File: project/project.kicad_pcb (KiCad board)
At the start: 6 copper layers, 45 x 115 mm, 235 parts, among them IC1 ESP32-C61-WROOM-1-N8R2, IC10 TLV320AIC3104IRHBR, IC11 TPA2005D1DGNR, IC12 MAX17262REWL+T, IC3 STPMIC1DPQR, IC4 ST1S31PUR, IC5 MCP23017-E_ML, IC6 TPS2117DRLR, IC7 ECMF02-2AMX6, IC8 TCPP01-M12, IC9 MT41K128M16JT-107_K, J1 Micro_SD_Card_Det2, J2 OMTP, Q2 STL11N3LLH6, SW1 PTS636SM43SMTR LFS, SW2 SW_DIP_x04, SW3 PTS636SM43SMTR LFS, U1 STM32MP135F, U2 USB C DRP, U3 MCP73831-2-OT, U5 EMIF06-MSD02N16, Y1 Crystal 24 MHz, Y2 Crystal 32.67 KHz

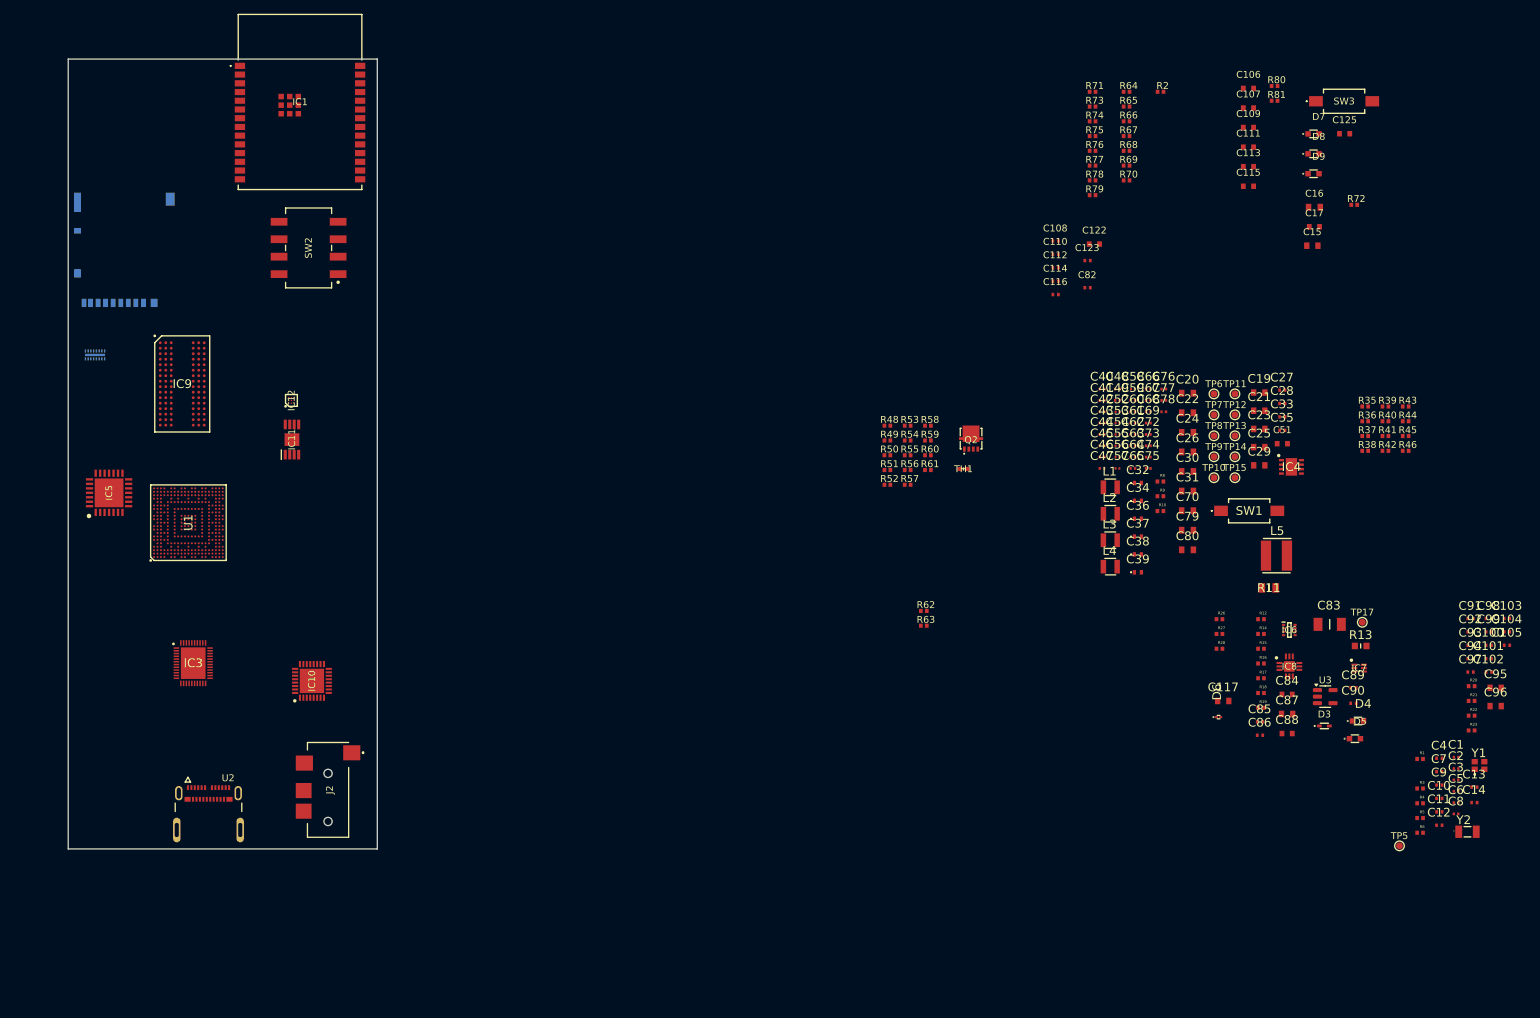
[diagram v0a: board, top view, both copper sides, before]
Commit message: schemtic is done, annotation set
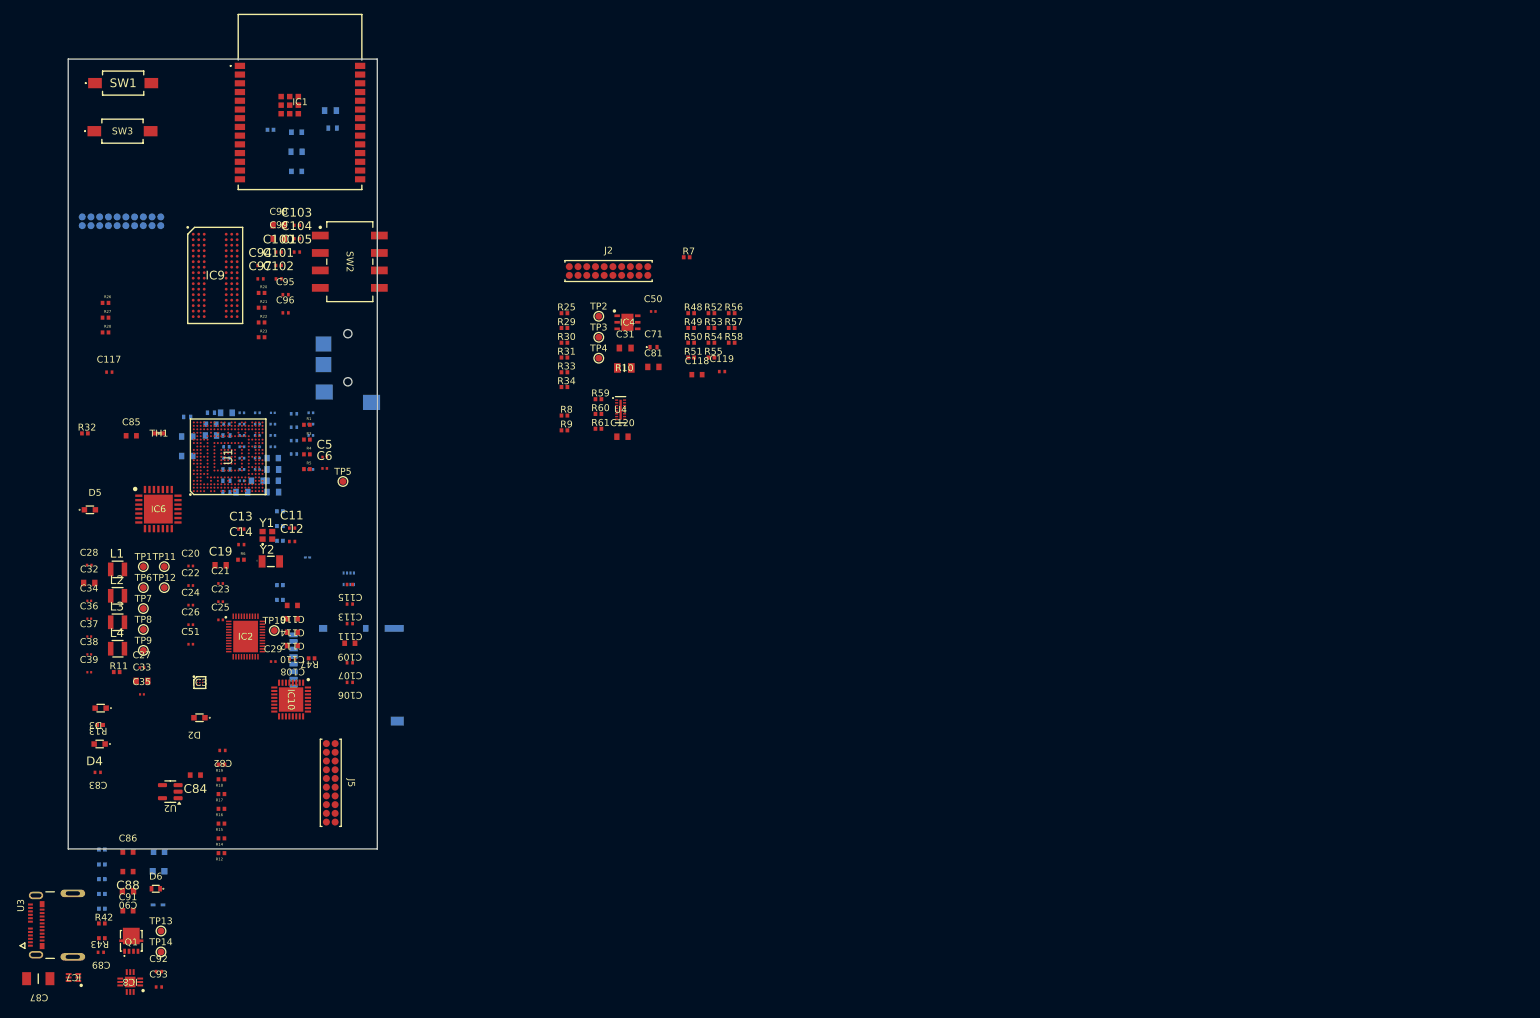
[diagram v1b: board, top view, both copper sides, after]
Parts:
- removed C122, C125: 100nF, bozi:GRM18_T10
- removed C123: 1uF, bozi:GRM15_T05
- removed C30: 22uF, bozi:GRM18_T20
- removed C57: 1nF, bozi:GRM03_T03
- removed IC11: TPA2005D1DGNR, bozi:SOP65P490X110-9N
- removed IC12: MAX17262REWL+T, bozi:BGA9C40P3X3_147X145X69
- removed L5: 2.2uH, bozi:INDPM4040X250N_edit
- removed Q2: STL11N3LLH6, bozi:STL20N6F7_edit
- removed R62, R63: 2.4K, bozi:RESC1005X37N_edit
- removed R64, R65, R66, R67, R68, R69, R70, R71, R72, R73, R74, R75, R76, R77, R78, R79, R80, R81: 0R, bozi:RESC1005X37N_edit
- removed TP15, TP17: TestPoint, TestPoint:TestPoint_Pad_D1.0mm
- removed U5: EMIF06-MSD02N16, bozi:MICROQFN16_1P25X3P55X0P4_STM_edit
- added C118: 100nF, bozi:GRM18_T10, F.Cu at (176.5, 78.5)
- added C119: 1uF, bozi:GRM15_T05, F.Cu at (180.2, 78.0)
- added C120: 10uF, bozi:GRT18_T15, F.Cu at (165.7, 87.5)
- added C18: 100nF, bozi:GRM18_T10, B.Cu at (118.2, 48.9)
- added C50: 1uF, bozi:GRM03_T09, F.Cu at (170.2, 69.2)
- added C71: 4.7uF, bozi:GRM15_T15, F.Cu at (170.2, 74.4)
- added C81: 10uF, bozi:GRT18_T15, F.Cu at (170.2, 77.3)
- added D1: TVS 22VWM 41VC, bozi:ESDA25P351U1M_edit, B.Cu at (123.5, 42.5)
- added D2: LED, bozi:LEDC1608X70N_edit, F.Cu at (104.1, 128.4)
- added IC2: STPMIC1DPQR, bozi:QFN40P500X600X80-45N-D_edit, F.Cu at (110.8, 116.6)
- added J3: CTIA, bozi:SJ23574ASMTTR, B.Cu at (126.0, 77.1)
- added J4: Micro_SD_Card_Det2, Connector_Card:microSD_HC_Hirose_DM3AT-SF-PEJM5, B.Cu at (125.5, 122.2)
- added J5: POGO header keypad & power, bozi:8552202030001101_edit, F.Cu at (123.2, 137.9)
- added Q1: STL11N3LLH6, bozi:STL20N6F7_edit, F.Cu at (94.2, 160.9)
- added R24: 100R, bozi:RESC1005X37N_edit, B.Cu at (115.8, 111.2)
- added R25: 100R, bozi:RESC1005X37N_edit, F.Cu at (157.2, 69.5)
- added R29: 10k, bozi:RESC1005X37N_edit, F.Cu at (157.2, 71.7)
- added R30: 10k, bozi:RESC1005X37N_edit, F.Cu at (157.2, 73.8)
- added R31: 1k, bozi:RESC1005X37N_edit, F.Cu at (157.2, 76.0)
- added R32: 1k, bozi:RESC1005X37N_edit, F.Cu at (87.4, 87.0)
- added R33: 1k, bozi:RESC1005X37N_edit, F.Cu at (157.2, 78.1)
- added R34: 1k, bozi:RESC1005X37N_edit, F.Cu at (157.2, 80.2)
- added R47: 240R, bozi:RESC1005X37N_edit, F.Cu at (120.4, 119.8)
- added R7: 0R, bozi:RESC1005X37N_edit, F.Cu at (175.0, 61.4)
- added TP1: TestPoint, TestPoint:TestPoint_Pad_D1.0mm, F.Cu at (95.9, 106.4)
- added TP2: TestPoint, TestPoint:TestPoint_Pad_D1.0mm, F.Cu at (162.2, 70.0)
- added TP3: TestPoint, TestPoint:TestPoint_Pad_D1.0mm, F.Cu at (162.2, 73.0)
- added TP4: TestPoint, TestPoint:TestPoint_Pad_D1.0mm, F.Cu at (162.2, 76.0)
- added U4: EMIF06-MSD02N16, bozi:MICROQFN16_1P25X3P55X0P4_STM_edit, F.Cu at (165.4, 83.6)
- C1, C10, C2, C3, C4, C41, C42, C43, C48, C49, C59, C60, C61, C62, C63, C64, C7, C8, C9, D8, R35: moved to B.Cu
- C106, C107: footprint bozi:GRM18_T10 -> bozi:GRM15_T05
- C108: value 1uF -> 100nF
- C110, C112, C114, C116: value 1uF -> 100nF; footprint bozi:GRM15_T05 -> bozi:GRM18_T10
- C111, C113, C115: value 100nF -> 1uF; footprint bozi:GRM18_T10 -> bozi:GRM15_T05
- C117: value 10uF -> 1uF; footprint bozi:GRT18_T15 -> bozi:GRM15_T05
- C15: value 10uF -> 22uF; footprint bozi:GRT18_T15 -> bozi:GRM18_T20; moved to B.Cu
- C16: value 22uF -> 100nF; footprint bozi:GRM18_T20 -> bozi:GRM18_T10; moved to B.Cu
- C17: value 100nF -> 10uF; footprint bozi:GRM18_T10 -> bozi:GRT18_T15; moved to B.Cu
- C20, C22, C24, C26: value 22uF -> 1uF; footprint bozi:GRM18_T20 -> bozi:GRM03_T09
- C21, C23, C25, C29: value 10uF -> 1uF; footprint bozi:GRT18_T15 -> bozi:GRM03_T09
- C27, C28: footprint bozi:GRM15_T05 -> bozi:GRM03_T09
- C32: value 4.7uF -> 10uF; footprint bozi:GRM15_T15 -> bozi:GRT18_T15
- C33: value 1uF -> 22uF; footprint bozi:GRM15_T05 -> bozi:GRM18_T20
- C34, C36, C37, C38, C39: value 4.7uF -> 1nF; footprint bozi:GRM15_T15 -> bozi:GRM03_T03
- C35: value 1uF -> 1nF; footprint bozi:GRM15_T05 -> bozi:GRM03_T03
- C40: value 1uF -> 1nF; footprint bozi:GRM03_T09 -> bozi:GRM03_T03; moved to B.Cu
- C44, C46: value 1uF -> 10uF; footprint bozi:GRM03_T09 -> bozi:GRT18_T15; moved to B.Cu
- C45, C47, C65, C66: value 1uF -> 22uF; footprint bozi:GRM03_T09 -> bozi:GRM18_T20; moved to B.Cu
- C51: value 100nF -> 1uF; footprint bozi:GRM18_T10 -> bozi:GRM03_T09
- C52, C53, C54, C55, C58: value 1nF -> 1uF; footprint bozi:GRM03_T03 -> bozi:GRM03_T09; moved to B.Cu
- C56: value 1nF -> 22uF; footprint bozi:GRM03_T03 -> bozi:GRM18_T20; moved to B.Cu
- C67, C69, C72: footprint bozi:GRM03_T09 -> bozi:GRM15_T05; moved to B.Cu
- C68, C73, C74, C75, C76: value 1uF -> 4.7uF; footprint bozi:GRM03_T09 -> bozi:GRM15_T15; moved to B.Cu
- C70: value 22uF -> 4.7uF; footprint bozi:GRM18_T20 -> bozi:GRM15_T15; moved to B.Cu
- C77: value 1uF -> 100nF; footprint bozi:GRM03_T09 -> bozi:GRM18_T10; moved to B.Cu
- C78: value 1uF -> 4.7uF; footprint bozi:GRM03_T09 -> bozi:GRM18_T15; moved to B.Cu
- C79: value 22uF -> 4.7uF; footprint bozi:GRM18_T20 -> bozi:GRM18_T15; moved to B.Cu
- C80: value 22uF -> 10uF; footprint bozi:GRM18_T20 -> bozi:GRT18_T15; moved to B.Cu
- C82: value 1uF -> 470pF; footprint bozi:GRM15_T05 -> bozi:GRT15_T05
- C83: value 220uF -> 1uF; footprint bozi:GRM31_T30 -> bozi:GRM15_T05
- C84: value 2.2uF -> 100nF
- C85: value 4.7uF -> 100nF; footprint bozi:GRM15_T05 -> bozi:GRM18_T10
- C86: value 4.7uF -> 2.2uF; footprint bozi:GRM15_T05 -> bozi:GRM18_T10
- C87: value 4.7uF -> 220uF; footprint bozi:GRM18_T15 -> bozi:GRM31_T30
- C88: value 100nF -> 100pF
- C89: value 470pF -> 1uF; footprint bozi:GRT15_T05 -> bozi:GRM15_T05
- C90: value 470pF -> 4.7uF; footprint bozi:GRT15_T05 -> bozi:GRM18_T15
- C91: footprint bozi:GRM15_T05 -> bozi:GRM18_T10
- C92, C93: value 100nF -> 470pF; footprint bozi:GRM15_T05 -> bozi:GRT15_T05
- C95, C96: value 10uF -> 100nF; footprint bozi:GRT18_T15 -> bozi:GRM15_T05
- C98, C99: value 100nF -> 10uF; footprint bozi:GRM15_T05 -> bozi:GRT18_T15
- D3: value BAT54KFILM -> LED; footprint bozi:SODFL1608X70N_edit -> bozi:LEDC1608X70N_edit
- D6: value ESDALC6V1-1U2 -> TVS 22VWM 41VC; footprint bozi:ESDALC6V11U2_edit -> bozi:ESDA25P351U1M_edit
- D7: value LED -> BAT54KFILM; footprint bozi:LEDC1608X70N_edit -> bozi:SODFL1608X70N_edit; moved to B.Cu
- D9: value LED -> ESDALC6V1-1U2; footprint bozi:LEDC1608X70N_edit -> bozi:ESDALC6V11U2_edit; moved to B.Cu
- IC3: value STPMIC1DPQR -> MAX17262REWL+T; footprint bozi:QFN40P500X600X80-45N-D_edit -> bozi:BGA9C40P3X3_147X145X69
- IC4: value ST1S31PUR -> LD39200PU33R; footprint bozi:SON65P300X300X100-9N-D_edit -> bozi:SON95P300X300X100-7N-D
- IC5: value MCP23017-E_ML -> TPS2117DRLR; footprint bozi:QFN65P600X600X100-29N-D_edit -> bozi:SOTFL50P160X60-8N; moved to B.Cu
- IC6: value TPS2117DRLR -> MCP23017-E_ML; footprint bozi:SOTFL50P160X60-8N -> bozi:QFN65P600X600X100-29N-D_edit
- J1: value Micro_SD_Card_Det2 -> POGO header 20 pin; footprint Connector_Card:microSD_HC_Hirose_DM3AT-SF-PEJM5 -> bozi:8552202030001101_edit
- J2: value OMTP -> POGO header display; footprint bozi:SJ23574ASMTTR -> bozi:8552202030001101_edit
- R1, R3: value 2.4K -> 2.4k
- R10: value 24k -> 100m; footprint bozi:RESC1005X37N_edit -> bozi:RESC2012X60N_edit
- R11: value 100m -> 0R; footprint bozi:RESC2012X60N_edit -> bozi:RESC1005X37N_edit
- R12, R23: value 240R -> 0R
- R13: value 1R -> 0R; footprint bozi:RESC1608X55N_edit -> bozi:RESC1005X37N_edit
- R14, R20, R21: value 10K -> 0R
- R15: value 47K -> 1k
- R16: value 47K -> 240R
- R17: value 2.4K -> 1k
- R18, R19: value 5.1K -> 0R
- R2: value 0R -> 2.4k; moved to B.Cu
- R22: value 100R -> 0R
- R26: value 10K -> 100R
- R27: value 10K -> 10k
- R28: value 100K -> 10k
- R36: value 100R -> 240R; moved to B.Cu
- R37: value 100R -> 1R; footprint bozi:RESC1005X37N_edit -> bozi:RESC1608X55N_edit; moved to B.Cu
- R38: value 1K -> 10k; moved to B.Cu
- R39: value 1K -> 2.4k; moved to B.Cu
- R4: value 3K -> 2.4k
- R40, R41: value 1K -> 47k; moved to B.Cu
- R42: value 10K -> 5.1k
- R43: value 100R -> 5.1k
- R44, R45: value 10K -> 10k; moved to B.Cu
- R46: value 10K -> 100R; moved to B.Cu
- R48: value 30R -> 1k
- R49, R50, R51, R52, R53, R54, R55, R56, R57, R58: value 30R -> 0R
- R5: value 240R -> 3k
- R59, R60: value 30R -> 10k
- R6: value 0R -> 240R
- R61: value 30R -> 100k
- R8: value 560R -> 0R
- R9: value 75k -> 10k
- TH1: value 10K NTC -> 10k NTC
- U2: value USB C DRP -> MCP73831-2-OT; footprint bozi:2012670005_edit -> Package_TO_SOT_SMD:SOT-23-5
- U3: value MCP73831-2-OT -> USB C DRP; footprint Package_TO_SOT_SMD:SOT-23-5 -> bozi:2012670005_edit
- moved R43 205.0 mm to (89.9, 160.5), turned to 180 degrees
- moved D7 202.2 mm to (98.1, 155.7)
- moved C91 200.1 mm to (93.7, 156.5)
- moved R39 199.1 mm to (89.9, 151.9), turned to 180 degrees
- moved R40 199.1 mm to (89.9, 154.1), turned to 180 degrees
- moved R41 199.1 mm to (89.9, 156.2), turned to 180 degrees
- moved R42 199.1 mm to (89.9, 158.3)
- moved C93 197.3 mm to (98.2, 167.6)
- moved C92 197.3 mm to (98.2, 165.3)
- moved D8 196.4 mm to (98.2, 148.0)
- moved R36 194.2 mm to (89.9, 147.6)
- moved R38 193.5 mm to (89.9, 149.8), turned to 180 degrees
- moved IC7 192.5 mm to (85.8, 166.2), turned to 180 degrees
- moved D5 187.2 mm to (88.2, 98.1)
- moved R37 186.8 mm to (98.2, 150.8)
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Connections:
- C104 pad 1: VREF_DDR -> VDD_DDR
- C105 pad 1: VREF_DDR -> VDD_DDR
- C106 pad 1: Net-(U4-SEL) -> VDD_DDR
- C107 pad 1: Net-(IC10-DRVDD_1) -> VREF_DDR
- C108 pad 1: Net-(IC10-DRVDD_1) -> VREF_DDR
- C109 pad 1: Net-(IC10-DRVDD_1) -> Net-(IC10-MIC2R/LINE2R)
- C109 pad 2: GNDREF -> Net-(IC10-MIC2L/LINE2L/MICDET)
- C111 pad 1: Net-(IC10-AVDD) -> Net-(IC10-DRVDD_1)
- C112 pad 1: Net-(IC10-AVDD) -> Net-(IC10-DRVDD_1)
- C113 pad 1: Net-(IC10-IOVDD) -> Net-(IC10-DRVDD_1)
- C114 pad 1: Net-(IC10-IOVDD) -> Net-(IC10-AVDD)
- C115 pad 1: Net-(IC10-DVDD) -> Net-(IC10-AVDD)
- C116 pad 1: Net-(IC10-DVDD) -> Net-(IC10-IOVDD)
- C117 pad 1: VDD_SD -> Net-(IC10-IOVDD)
- C15 pad 1: VDD_3V3 -> Net-(IC1-3V3)
- C17 pad 1: Net-(IC1-3V3) -> 3V3_AO
- C19 pad 1: 5V_VIN -> VSYS
- C20 pad 1: VDD_CPU -> VDD
- C21 pad 1: 5V_VIN -> VDD
- C22 pad 1: VDD_DDR -> VDD
- C23 pad 1: 5V_VIN -> VDD
- C25 pad 1: 5V_VIN -> VDD
- C26 pad 1: VDD_CORE -> VDD
- C27 pad 1: VREF_DDR -> VDD
- C28 pad 1: 5V_VIN -> VDD
- C29 pad 1: 5V_VIN -> VDD
- C31 pad 1: 3V3_AO -> VDD_CPU
- C32 pad 1: VDD_ADC -> VSYS
- C33 pad 1: 5V_VIN -> VDD_DDR
- C34 pad 1: Net-(IC3-LDO2OUT) -> VDD_DDR
- C35 pad 1: 5V_VIN -> VDD_DDR
- C36 pad 1: VDD_SD -> VDD_DDR
- C37 pad 1: GNDREF -> VDD_DDR
- C37 pad 2: 5V_VIN -> GNDREF
- C38 pad 1: GNDREF -> VDD_DDR
- C38 pad 2: Net-(IC3-INTLDO) -> GNDREF
- C39 pad 1: Net-(IC3-LDO4OUT) -> VDD_DDR
- C40 pad 1: VDD -> VDD_DDR
- C41 pad 1: VDD -> VDD_DDR
- C42 pad 1: VDD -> VDD_DDR
- C43 pad 1: VDD -> VDD_DDR
- C44 pad 1: VDD -> VSYS
- C46 pad 1: VDD -> VSYS
- C47 pad 1: VDD -> VDD_CORE
- C48 pad 1: VDD -> VDD_CORE
- C49 pad 1: VDD -> VDD_CORE
- C51 pad 1: Net-(IC3-PONKEYN) -> VDD_CORE
- C52 pad 1: VDD_DDR -> VDD_CORE
- C53 pad 1: VDD_DDR -> VDD_CORE
- C54 pad 1: VDD_DDR -> VDD_CORE
- C55 pad 1: VDD_DDR -> VDD_CORE
- C56 pad 1: VDD_DDR -> VDD_CORE
- C58 pad 1: VDD_DDR -> VDD_CPU
- C59 pad 1: VDD_DDR -> VDD_CPU
- C60 pad 1: VDD_DDR -> VDD_CPU
- C61 pad 1: VDD_DDR -> VDD_CPU
- C62 pad 1: VDD_CORE -> VDD_CPU
- C63 pad 1: VDD_CORE -> VDD_CPU
- C64 pad 1: VDD_CORE -> VDD_CPU
- C65 pad 1: VDD_CORE -> VDD_CPU
- C66 pad 1: VDD_CORE -> VDD_CPU
- C67 pad 1: VDD_CORE -> VREF_DDR
- C68 pad 1: VDD_CORE -> VDD_ADC
- C69 pad 1: VDD_CORE -> VSYS
- C70 pad 1: VDD_CORE -> VDD_CODEC
- C72 pad 1: VDD_CPU -> VSYS
- C73 pad 1: VDD_CPU -> VDD_SD
- C74 pad 1: VDD_CPU -> GNDREF
- C74 pad 2: GNDREF -> VSYS
- C75 pad 1: VDD_CPU -> GNDREF
- C75 pad 2: GNDREF -> Net-(IC2-INTLDO)
- C76 pad 1: VDD_CPU -> Net-(IC2-LDO4OUT)
- C77 pad 1: VDD_CPU -> Net-(IC2-PONKEYN)
- C78 pad 1: VDD_CPU -> Net-(D2-A)
- C78 pad 2: GNDREF -> GND
- C79 pad 1: VDD_CPU -> Net-(U2-V_{BAT})
- C79 pad 2: GNDREF -> GND
- C80 pad 1: VDD_CPU -> 3V3_AO
- C82 pad 1: Net-(D2-K) -> Net-(IC3-REG)
- C83 pad 1: 5V_VIN -> Net-(IC6-VDD)
- C84 pad 1: Net-(IC8-GATE) -> Net-(IC6-VDD)
- C84 pad 2: Net-(D2-K) -> GNDREF
- C85 pad 1: Net-(BT1-+) -> /GPIO & IO expander/NRST
- C85 pad 2: GND -> GNDREF
- C86 pad 1: Net-(D5-A) -> Net-(IC8-GATE)
- C86 pad 2: GND -> Net-(D6-K)
- C87 pad 1: GNDREF -> 5V_VIN
- C87 pad 2: Net-(C87-Pad2) -> GNDREF
- C88 pad 1: GNDREF -> Net-(D6-K)
- C88 pad 2: Net-(D3-K) -> GND
- C89 pad 1: /USB C DRP/USB_CC1 -> Net-(D6-K)
- C89 pad 2: GNDREF -> GND
- C90 pad 1: /USB C DRP/USB_CC2 -> GNDREF
- C90 pad 2: GNDREF -> Net-(C90-Pad2)
- C91 pad 1: VDD_DDR -> GNDREF
- C91 pad 2: GNDREF -> Net-(D7-K)
- C92 pad 1: VDD_DDR -> /USB C DRP/USB_CC1
- C93 pad 1: VDD_DDR -> /USB C DRP/USB_CC2
- D3 pad 1: Net-(D3-K) -> GNDREF
- D3 pad 2: Net-(D2-K) -> Net-(D3-A)
- D5 pad 1: Net-(D5-K) -> GNDREF
- D6 pad 1: /MPU/SDMMC1_DETECT -> Net-(D6-K)
- D6 pad 2: GNDREF -> GND
- D7 pad 1: GNDREF -> Net-(D7-K)
- D7 pad 2: Net-(D7-A) -> Net-(D6-K)
- D9 pad 1: GNDREF -> /MPU/SDMMC1_GPIO0
- D9 pad 2: Net-(D9-A) -> GNDREF
- IC10 pad 1: Net-(IC10-MCLK) -> /MPU/RCC_MCO_1
- IC4 pad 1: 5V_VIN -> 3V3_AO
- IC4 pad 2: VDD -> 3V3_AO
- IC4 pad 3: Net-(IC4-FB) -> GNDREF
- IC4 pad 4: GNDREF -> /MPU/REG_3V3_GPIO0
- IC4 pad 5: Net-(IC4-PG) -> VSYS
- IC4 pad 6: 5V_VIN -> VSYS
- IC4 pad 7: Net-(IC4-SW) -> GNDREF
- IC5 pad 1: /GPIO & IO expander/GPB4 -> GNDREF
- IC5 pad 2: /GPIO & IO expander/GPB5 -> Net-(IC5-VOUT_1)
- IC5 pad 3: /GPIO & IO expander/DIP1 -> Net-(IC5-VIN1)
- IC5 pad 4: /GPIO & IO expander/LD3 -> GNDREF
- IC5 pad 5: 3V3_AO -> GNDREF
- IC5 pad 6: GNDREF -> Net-(IC5-VIN2)
- IC5 pad 7: unconnected-(IC5-NC_1-Pad7) -> Net-(IC5-VOUT_1)
- IC5 pad 8: /GPIO & IO expander/IO_EX_I2C_SCL -> /MPU/VSOURCE_GPIO0
- IC6 pad 1: GNDREF -> /GPIO & IO expander/GPB4
- IC6 pad 2: Net-(IC6-VOUT_1) -> /GPIO & IO expander/GPB5
- IC6 pad 3: Net-(IC6-MODE) -> /GPIO & IO expander/DIP1
- IC6 pad 4: Net-(IC6-PR1) -> /GPIO & IO expander/LD3
- IC6 pad 5: Net-(IC6-MODE) -> Net-(IC6-VDD)
- IC6 pad 6: Net-(IC6-VIN2) -> GNDREF
- IC6 pad 7: Net-(IC6-VOUT_1) -> unconnected-(IC6-NC_1-Pad7)
- IC6 pad 8: /MPU/VSOURCE_GPIO0 -> /GPIO & IO expander/IO_EX_I2C_SCL
- IC8 pad 8: Net-(D3-K) -> Net-(D7-K)
- J1 pad 1: Net-(J1-DAT2) -> /GPIO & IO expander/SAI_DAT
- J1 pad 10: GNDREF -> /GPIO & IO expander/T_JTDI
- J1 pad 11: GNDREF -> Net-(J1-Pad11)
- J1 pad 2: Net-(J1-DAT3/CD) -> /GPIO & IO expander/SAI_CLK
- J1 pad 3: Net-(J1-CMD) -> VDD
- J1 pad 4: VDD_SD -> /GPIO & IO expander/T_JTMS/T_SWDIO
- J1 pad 5: Net-(J1-CLK) -> GNDREF
- J1 pad 6: GNDREF -> /GPIO & IO expander/T_JCLK/T_SWCLK
- J1 pad 7: Net-(J1-DAT0) -> GNDREF
- J1 pad 8: Net-(J1-DAT1) -> /GPIO & IO expander/T_JTDO/T_SWO
- J1 pad 9: /MPU/SDMMC1_DETECT -> unconnected-(J1-Pad9)
- J2 pad 1: Net-(J2-GND) -> GNDREF
- J2 pad 2: Net-(J2-MIC) -> GNDREF
- J2 pad 3: Net-(IC10-HPROUT) -> /Display/LCD_DAT7
- J2 pad 4: Net-(IC10-HPLOUT) -> /Display/LCD_RDX
- L1 pad 2: Net-(IC3-VLX1) -> Net-(IC2-VLX1)
- L2 pad 2: Net-(IC3-VLX2) -> Net-(IC2-VLX2)
- L3 pad 1: Net-(IC3-VLX3) -> Net-(IC2-VLX3)
- L4 pad 1: Net-(IC3-VLX4) -> Net-(IC2-VLX4)
- R1 pad 1: VDD -> /GPIO & IO expander/IO_EX_I2C_SCL
- R1 pad 2: /MPU/I2C3_SCL -> VDD
- R10 pad 1: GNDREF -> Net-(IC2-LDO4OUT)
- R10 pad 2: Net-(IC4-FB) -> VDD_USB
- R11 pad 1: Net-(IC3-LDO4OUT) -> Net-(U2-V_{BAT})
- R11 pad 2: VDD_USB -> VBAT
- R12 pad 2: Net-(D4-A) -> Net-(D2-A)
- R13 pad 1: Net-(C87-Pad2) -> Net-(U2-V_{BAT})
- R13 pad 2: Net-(D2-K) -> Net-(IC3-BATT)
- R14 pad 1: Net-(D2-K) -> Net-(IC3-SYS)
- R14 pad 2: Net-(IC8-VBUS_CTRL) -> VBAT
- R15 pad 1: /MPU/USB_PWR_GPIO0 -> Net-(U2-PROG)
- R15 pad 2: Net-(IC8-CC1) -> Net-(R15-Pad2)
- R16 pad 1: /MPU/USB_PWR_GPIO1 -> Net-(D2-K)
- R16 pad 2: Net-(IC8-CC2) -> Net-(U2-STAT)
- R17 pad 1: Net-(IC8-VBUS_CTRL) -> Net-(R15-Pad2)
- R17 pad 2: GNDREF -> GND
- R18 pad 1: Net-(IC8-CC2) -> VBAT
- R18 pad 2: GNDREF -> VSYS
- R19 pad 1: Net-(IC8-CC1) -> 5V_VIN
- R19 pad 2: GNDREF -> VSYS
- R2 pad 1: VDD_3V3 -> /GPIO & IO expander/IO_EX_I2C_SDA
- R2 pad 2: Net-(IC1-3V3) -> VDD
- R20 pad 1: /DDR3L/~{DDR_RESET} -> 5V_VIN
- R20 pad 2: GNDREF -> Net-(IC5-VIN2)
- R21 pad 1: /DDR3L/DDR_CKE -> VSYS
- R21 pad 2: GNDREF -> Net-(IC5-VOUT_1)
- R22 pad 1: /DDR3L/DDR_CLKP -> VBAT
- R22 pad 2: /DDR3L/DDR_CLKN -> Net-(IC5-VIN1)
- R23 pad 1: GNDREF -> 3V3_AO
- R23 pad 2: Net-(IC9-ZQ) -> Net-(IC6-VDD)
- R26 pad 1: VDD_SD -> /GPIO & IO expander/LD3
- R26 pad 2: /MPU/SDMMC1_CK -> Net-(D5-A)
- R27 pad 1: /MPU/SDMMC1_CK -> Net-(IC6-A0)
- R27 pad 2: GNDREF -> 3V3_AO
- R28 pad 1: VDD -> Net-(IC6-A1)
- R28 pad 2: /MPU/SDMMC1_DETECT -> GNDREF
- R35 pad 1: /GPIO & IO expander/LD1 -> Net-(J1-Pad11)
- R35 pad 2: Net-(D7-A) -> GNDREF
- R36 pad 1: /GPIO & IO expander/LD2 -> 5V_VIN
- R37 pad 1: /GPIO & IO expander/LD3 -> Net-(C90-Pad2)
- R37 pad 2: Net-(D9-A) -> Net-(D6-K)
- R38 pad 1: VDD -> Net-(D6-K)
- R38 pad 2: Net-(R38-Pad2) -> Net-(IC8-VBUS_CTRL)
- R39 pad 1: VDD -> Net-(IC8-VBUS_CTRL)
- R39 pad 2: Net-(R39-Pad2) -> GNDREF
- R4 pad 1: Net-(U1E-USB_RREF) -> VDD
- R4 pad 2: GNDREF -> /MPU/I2C3_SCL
- R40 pad 1: VDD -> /MPU/USB_PWR_GPIO0
- R40 pad 2: Net-(R40-Pad2) -> Net-(IC8-CC1)
- R41 pad 1: VDD -> /MPU/USB_PWR_GPIO1
- R41 pad 2: Net-(R41-Pad2) -> Net-(IC8-CC2)
- R42 pad 1: VDD -> Net-(IC8-CC2)
- R42 pad 2: Net-(D10-K) -> GNDREF
- R43 pad 1: Net-(J3-Pad11) -> Net-(IC8-CC1)
- R44 pad 1: Net-(IC5-A0) -> /DDR3L/~{DDR_RESET}
- R44 pad 2: 3V3_AO -> GNDREF
- R45 pad 1: Net-(IC5-A1) -> /DDR3L/DDR_CKE
- R46 pad 1: Net-(IC5-A2) -> /DDR3L/DDR_CLKP
- R46 pad 2: GNDREF -> /DDR3L/DDR_CLKN
- R48 pad 1: Net-(J6-Pad15) -> Net-(IC10-MICBIAS)
- R48 pad 2: /Display/LCD_DAT7 -> Net-(IC10-MIC2L/LINE2L/MICDET)
- R49 pad 1: Net-(J6-Pad14) -> Net-(J3-MIC)
- R49 pad 2: /Display/LCD_DAT6 -> Net-(IC10-HPLCOM)
- R5 pad 1: GNDREF -> Net-(U1E-USB_RREF)
- R5 pad 2: Net-(U1D-DDR_ZQ) -> GNDREF
- R50 pad 1: Net-(J6-Pad13) -> Net-(J3-GND)
- R50 pad 2: /Display/LCD_DAT5 -> Net-(IC10-MIC2L/LINE2L/MICDET)
- R51 pad 1: Net-(J6-Pad12) -> Net-(J3-MIC)
- R51 pad 2: /Display/LCD_DAT4 -> Net-(IC10-MIC2L/LINE2L/MICDET)
- R52 pad 1: Net-(J6-Pad11) -> Net-(J3-GND)
- R52 pad 2: /Display/LCD_DAT3 -> Net-(IC10-HPLCOM)
- R53 pad 1: Net-(J6-Pad10) -> Net-(IC10-DRVDD_1)
- R53 pad 2: /Display/LCD_DAT2 -> 3V3_AO
- R54 pad 1: Net-(J6-Pad9) -> Net-(IC10-AVDD)
- R54 pad 2: /Display/LCD_DAT1 -> 3V3_AO
- R55 pad 1: Net-(J6-Pad8) -> Net-(IC10-DVDD)
- R55 pad 2: /Display/LCD_DAT0 -> VDD_CODEC
- R56 pad 1: Net-(J6-Pad7) -> Net-(IC10-IOVDD)
- R56 pad 2: /Display/LCD_RDX -> 3V3_AO
- R57 pad 1: Net-(J6-Pad6) -> /Keypad/EXTRA_GPIO1
- R57 pad 2: /Display/LCD_WRX -> Net-(IC10-RIGHT_LOP)
- R58 pad 1: Net-(J6-Pad5) -> /Keypad/EXTRA_GPIO0
- R58 pad 2: /Display/LCD_D/CX -> Net-(IC10-RIGHT_LOM)
- R59 pad 1: Net-(J6-Pad4) -> VDD_SD
- R59 pad 2: /Display/LCD_CSX -> /MPU/SDMMC1_CK
- R6 pad 1: Net-(C14-Pad1) -> GNDREF
- R6 pad 2: /MPU/OUT_32K67 -> Net-(U1D-DDR_ZQ)
- R60 pad 1: Net-(J6-Pad3) -> /MPU/SDMMC1_CK
- R60 pad 2: /Display/LCD_TE -> GNDREF
- R61 pad 1: Net-(J6-Pad2) -> VDD
- R61 pad 2: /Display/LCD_RESX -> /MPU/SDMMC1_GPIO0
- R8 pad 1: Net-(IC4-PG) -> 3V3_AO
- R8 pad 2: 3V3_AO -> Net-(IC1-3V3)
- R9 pad 1: Net-(IC4-FB) -> 3V3_AO
- R9 pad 2: 3V3_AO -> /MPU/WIFI_BLE_GPIO0
- SW1 pad 1: Net-(IC3-PONKEYN) -> Net-(IC2-PONKEYN)
- SW2 pad 1: Net-(R38-Pad2) -> Net-(R31-Pad2)
- SW2 pad 2: Net-(R39-Pad2) -> Net-(R32-Pad2)
- SW2 pad 3: Net-(R40-Pad2) -> Net-(R33-Pad2)
- SW2 pad 4: Net-(R41-Pad2) -> Net-(R34-Pad2)
- SW3 pad 1: Net-(D10-K) -> /GPIO & IO expander/NRST
- TH1 pad 1: Net-(IC12-TH) -> Net-(IC3-TH)
- TP10 pad 1: 3V3_AO -> VDD_SD
- TP11 pad 1: VREF_DDR -> Net-(IC2-LDO4OUT)
- TP12 pad 1: VDD_ADC -> 3V3_AO
- TP13 pad 1: Net-(IC3-LDO2OUT) -> Net-(D6-K)
- TP14 pad 1: VDD_SD -> 5V_VIN
- TP5 pad 1: Net-(U1E-PWR_CPU_ON) -> VDD_CORE
- TP6 pad 1: VDD_CPU -> VREF_DDR
- TP7 pad 1: VDD_DDR -> VDD_ADC
- TP8 pad 1: VDD -> VDD_CODEC
- TP9 pad 1: VDD_CORE -> Net-(IC2-LDO2OUT)
- U1 pad A15: /Display/LCD_RESX -> /Display/LCD_GPIO0
- U1 pad A16: /MPU/SDMMC1_DETECT -> /Display/LCD_RESX
- U1 pad B14: /Display/LCD_TE -> /Display/LCD_GPIO1
- U1 pad B15: unconnected-(U1B-PB15-PadB15) -> /Display/LCD_TE
- U1 pad B16: unconnected-(U1B-PB14-PadB16) -> /MPU/SDMMC1_GPIO0
- U1 pad G2: unconnected-(U1C-PG10-PadG2) -> /MPU/REG_3V3_GPIO0
- U1 pad J2: /MPU/SAI1_CK1 -> /GPIO & IO expander/SAI_CLK
- U1 pad J3: /MPU/SAI1_D1 -> /GPIO & IO expander/SAI_DAT
- U1 pad T4: unconnected-(U1B-PA13-PadT4) -> /MPU/RCC_MCO_1

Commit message: PCB design, finished RAM, audio, battery fuel gauge and charger, PMIC, USB C power
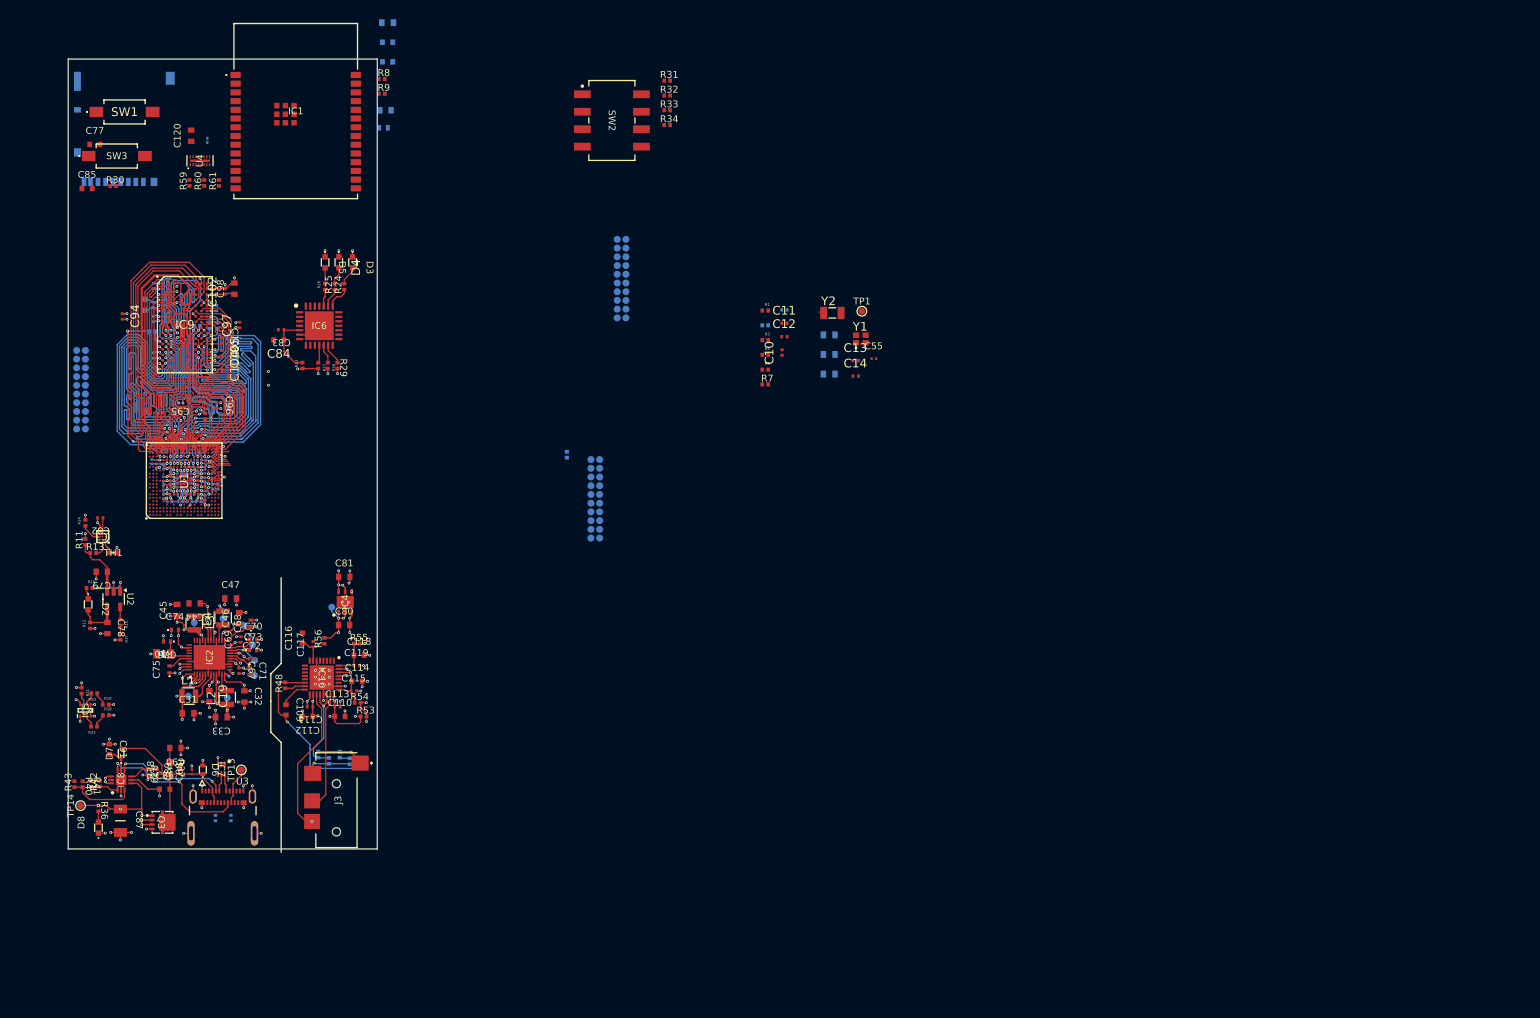
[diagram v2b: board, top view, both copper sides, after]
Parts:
- removed Q1: STL11N3LLH6, bozi:STL20N6F7_edit
- removed R57, R58: 0R, bozi:RESC1005X37N_edit
- removed TP9: TestPoint, TestPoint:TestPoint_Pad_D1.0mm
- added Q3: STL11N3LLH6, bozi:STL20N6F7_edit, F.Cu at (98.7, 143.6)
- C10, C44, C45, C46, C47, C55, C67, C68, C69, C70, C72, C73, C74, C75, C76, C77, C78, C79, C80, D7, D8, R24, R36, R37, R38, R39, R40, R41: moved to F.Cu
- C100, C101, C103, C106, C107, C20, C21, C22, C23, C24, C25, C26, C27, C28, C29, C34, C35, C36, C37, C38, C39, C5, C50, C51, C6, C92, C93, C99, J2, J5, R47, R49, R50, R51, R52, TP10, TP11, TP12, TP2, TP3, TP4, TP5, TP6, TP7, TP8: moved to B.Cu
- C88: footprint bozi:GRM18_T10 -> bozi:GRM03_T09
- IC10: footprint bozi:QFN50P500X500X100-33N-D -> bozi:QFN50P500X500X100-33N-D_edit
- IC3: footprint bozi:BGA9C40P3X3_147X145X69 -> bozi:BGA9C40P3X3_147X145X69_edit
- IC4: footprint bozi:SON95P300X300X100-7N-D -> bozi:SON95P300X300X100-7N-D_edit
- IC5: footprint bozi:SOTFL50P160X60-8N -> bozi:SOTFL50P160X60-8N_edit; moved to F.Cu
- IC7: footprint bozi:SON50P150X170X55-6N-D -> bozi:SON50P150X170X55-6N-D_edit
- IC8: footprint bozi:QFN50P300X300X100-13N-D -> bozi:QFN50P300X300X100-13N-D_edit
- J3: footprint bozi:SJ23574ASMTTR -> bozi:SJ23574ASMTTR_edit; moved to F.Cu
- moved TP1 111.0 mm to (200.6, 69.2)
- moved R32 98.0 mm to (172.2, 37.8)
- moved C13 92.8 mm to (199.7, 76.4)
- moved C14 92.8 mm to (199.7, 78.7)
- moved C55 91.2 mm to (202.3, 76.1), turned to 0 degrees
- moved Y1 91.0 mm to (200.4, 73.3)
- moved Y2 89.4 mm to (196.2, 69.5)
- moved C66 87.9 mm to (195.8, 78.4)
- moved C65 87.8 mm to (195.8, 75.5)
- moved C56 85.9 mm to (195.8, 72.7)
- moved J4 85.9 mm to (93.2, 42.7), turned to 0 degrees
- moved R52 85.7 mm to (123.0, 134.7), turned to 90 degrees
- moved J5 84.7 mm to (165.6, 64.5), turned to 90 degrees
- moved C31 82.9 mm to (102.5, 127.8)
- moved R49 82.5 mm to (121.4, 133.8), turned to -90 degrees
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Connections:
- C44 pad 1: VSYS -> GNDREF
- C44 pad 2: GNDREF -> VSYS
- C78 pad 2: GND -> GNDREF
- C79 pad 2: GND -> GNDREF
- C82 pad 2: GND -> GNDREF
- IC10 pad 29: Net-(IC10-RIGHT_LOP) -> /Keypad/EXTRA_GPIO1
- IC10 pad 30: Net-(IC10-RIGHT_LOM) -> /Keypad/EXTRA_GPIO0
- IC3 pad C3: GND -> GNDREF
- IC6 pad 1: /GPIO & IO expander/GPB4 -> /GPIO & IO expander/GPB3
- IC6 pad 2: /GPIO & IO expander/GPB5 -> /GPIO & IO expander/GPB4
- IC6 pad 22: /GPIO & IO expander/GPA5 -> /GPIO & IO expander/LD1
- IC6 pad 23: /GPIO & IO expander/LD1 -> /GPIO & IO expander/LD2
- IC6 pad 24: /GPIO & IO expander/LD2 -> /GPIO & IO expander/LD3
- IC6 pad 25: /GPIO & IO expander/GPB0 -> /GPIO & IO expander/GPA5
- IC6 pad 26: /GPIO & IO expander/GPB1 -> /GPIO & IO expander/GPB0
- IC6 pad 27: /GPIO & IO expander/GPB2 -> /GPIO & IO expander/GPB1
- IC6 pad 28: /GPIO & IO expander/GPB3 -> /GPIO & IO expander/GPB2
- IC6 pad 3: /GPIO & IO expander/DIP1 -> /GPIO & IO expander/GPB5
- IC6 pad 4: /GPIO & IO expander/LD3 -> /GPIO & IO expander/DIP1
- IC7 pad 1: /MPU/USB_D1_P -> /MPU/USB_D1_N
- IC7 pad 2: /MPU/USB_D1_N -> /MPU/USB_D1_P
- R17 pad 2: GND -> GNDREF
- TH1 pad 2: GND -> GNDREF
- TP11 pad 1: Net-(IC2-LDO4OUT) -> VDD_USB
- U2 pad 2: GND -> GNDREF
- U3 pad A1: GND -> GNDREF
- U3 pad A12: GND -> GNDREF
- U3 pad A6: Net-(IC7-D+) -> Net-(IC7-D-)
- U3 pad A7: Net-(IC7-D-) -> Net-(IC7-D+)
- U3 pad B1: GND -> GNDREF
- U3 pad B12: GND -> GNDREF
- U3 pad B6: Net-(IC7-D+) -> Net-(IC7-D-)
- U3 pad B7: Net-(IC7-D-) -> Net-(IC7-D+)
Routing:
- net GNDREF: track 0.00 -> 224.3 mm, vias 0 -> 144
- net VDD_DDR: track 0.00 -> 57.2 mm, vias 0 -> 29
- net /DDR3L/DDR_DQ1: track 0.00 -> 43.1 mm
- net /DDR3L/DDR_CLKN: track 0.00 -> 43.1 mm, vias 0 -> 2
- net /DDR3L/DDR_CLKP: track 0.00 -> 42.9 mm
- net /DDR3L/DDR_DQ4: track 0.00 -> 42.8 mm
- net /DDR3L/DDR_DQ7: track 0.00 -> 42.2 mm
- net /DDR3L/DDR_DQS0P: track 0.00 -> 41.9 mm
- net /DDR3L/DDR_DQS0N: track 0.00 -> 41.8 mm
- net /DDR3L/DDR_DQ2: track 0.00 -> 41.7 mm
- net /DDR3L/DDR_DQ5: track 0.00 -> 41.6 mm
- net /DDR3L/DDR_DQM0: track 0.00 -> 41.5 mm
- net /DDR3L/DDR_DQ0: track 0.00 -> 41.2 mm
- net /DDR3L/DDR_DQ3: track 0.00 -> 40.8 mm
- net /DDR3L/~{DDR_CS}: track 0.00 -> 40.7 mm, vias 0 -> 2
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- added copper zone on In1.Cu, net GNDREF
- added copper zone on In4.Cu, net GNDREF
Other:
- board text added: "CTIA"
- board text added: "OMTP"
